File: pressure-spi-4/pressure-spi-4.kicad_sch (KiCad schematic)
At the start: 13 parts, among them J1 Conn_01x08_Male, U1 TruStability_SPI_RR, U2 TruStability_SPI_RR, U3 TruStability_SPI_RR, U4 TruStability_SPI_RN

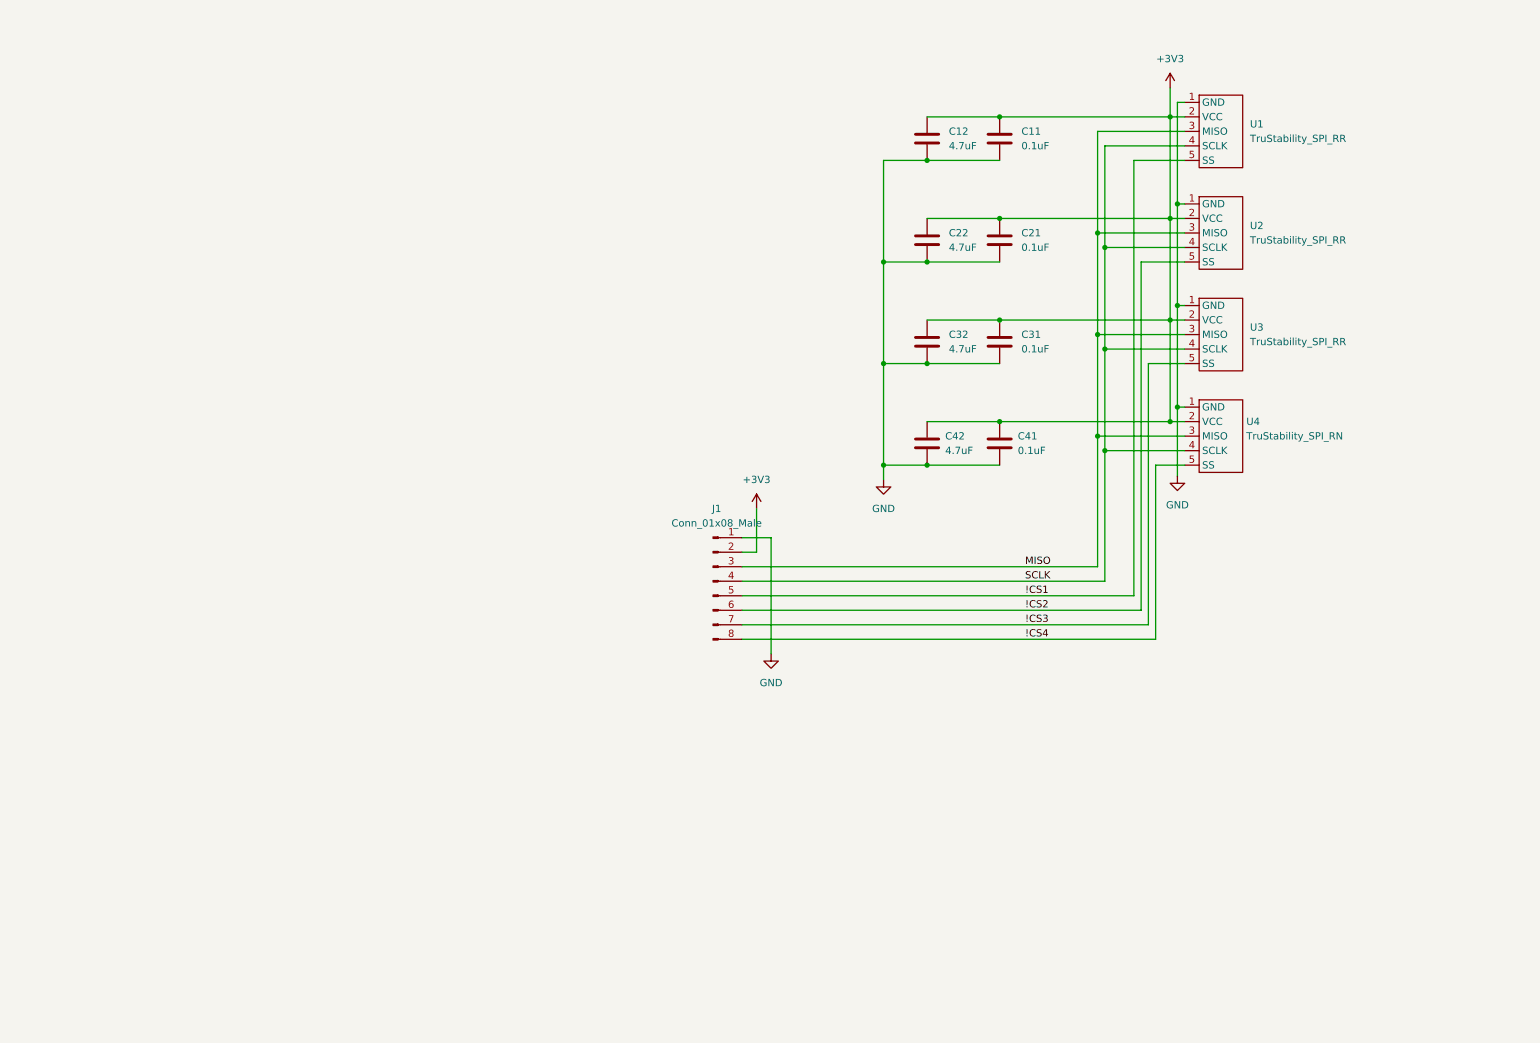
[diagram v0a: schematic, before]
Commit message: Designed and routed board.
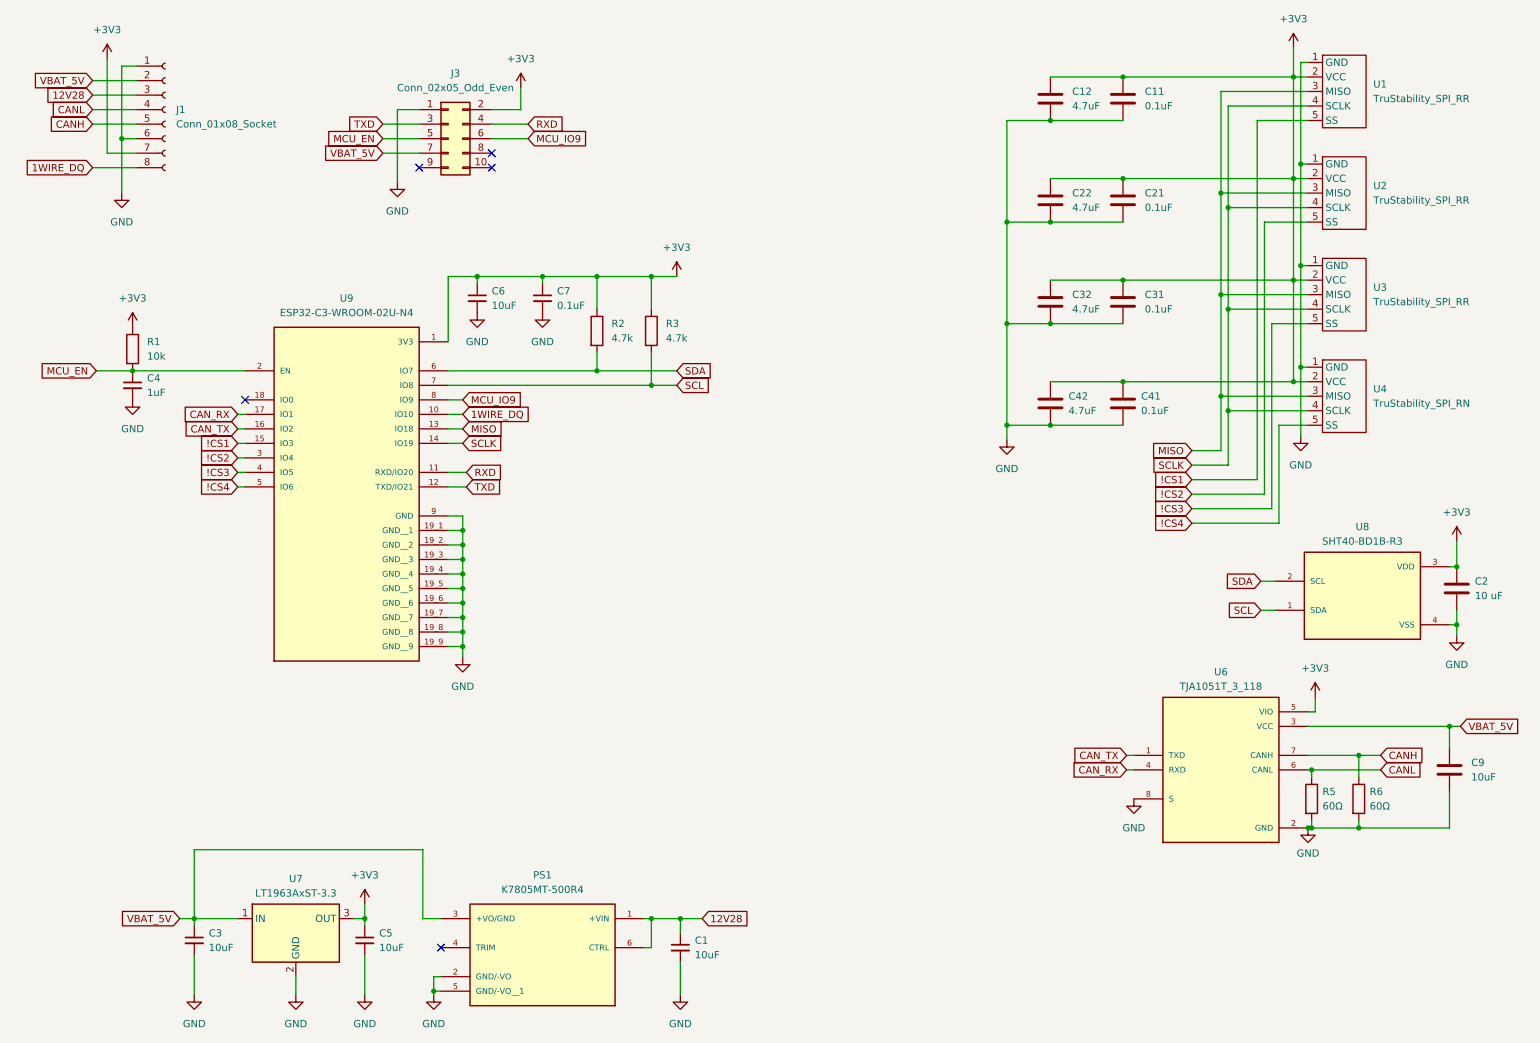
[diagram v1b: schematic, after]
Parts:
- removed J1: Conn_01x08_Male, airball-hardware:JST_SH_BM08B-SRSS-TB_1x08-1MP_P1.00mm_Vertical, symbol Connector:Conn_01x08_Male
- added C1, C3, C5, C6: 10uF, Capacitor_SMD:C_0603_1608Metric, symbol Device:C_Small
- added C2: 10 uF, Capacitor_SMD:C_0603_1608Metric, symbol Device:C
- added C4: 1uF, Capacitor_SMD:C_0603_1608Metric, symbol Device:C_Small
- added C7: 0.1uF, Capacitor_SMD:C_0603_1608Metric, symbol Device:C_Small
- added C9: 10uF, Capacitor_SMD:C_0603_1608Metric, symbol Device:C
- added J1: Conn_01x08_Socket, Connector_PinHeader_1.27mm:PinHeader_1x08_P1.27mm_Vertical, symbol Connector:Conn_01x08_Socket
- added J3: Conn_02x05_Odd_Even, Connector_PinHeader_1.27mm:PinHeader_2x05_P1.27mm_Vertical, symbol Connector_Generic:Conn_02x05_Odd_Even
- added PS1: K7805MT-500R4, airball-hardware:CONV_K7805MT-500R4, symbol airball-hardware:K7805MT-500R4
- added R1: 10k, Resistor_SMD:R_0603_1608Metric, symbol Device:R
- added R2, R3: 4.7k, Resistor_SMD:R_0603_1608Metric, symbol Device:R
- added R5, R6: 60Ω, Resistor_SMD:R_0603_1608Metric, symbol Device:R
- added U6: TJA1051T_3_118, airball-hardware:TJA1051T_3_118, symbol airball-hardware:TJA1051T_3_118
- added U7: LT1963AxST-3.3, Package_TO_SOT_SMD:SOT-223-3_TabPin2, symbol Regulator_Linear:LT1963AxST-3.3
- added U8: SHT40-BD1B-R3, airball-hardware:SHT4X humidity sensor, symbol airball-hardware:SHT40-BD1B-R3 humidity sensor
- added U9: ESP32-C3-WROOM-02U-N4, airball-hardware:XCVR_ESP32-C3-WROOM-02U-N4, symbol airball-hardware:ESP32-C3-WROOM-02U-N4
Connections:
- net !CS1: now also U9.15 (IO3)
- net !CS2: now also U9.3 (IO4)
- net !CS3: now also U9.4 (IO5)
- net !CS4: now also U9.5 (IO6)
- net +3V3: now also C2.1, C5.1, C6.1, C7.1, J1.7 (Pin_7), J3.2 (Pin_2), R1.1, R2.1, R3.1, U6.5 (VIO), U7.3 (OUT), U8.3 (VDD), U9.1 (3V3)
- net GND: now also C1.2, C2.2, C3.2, C4.2, C5.2, C6.2, C7.2, C9.2, J1.1 (Pin_1), J1.6 (Pin_6), J3.1 (Pin_1), PS1.2 (GND/-VO), PS1.5 (GND/-VO__1), R5.2, R6.2, U6.2 (GND), U6.8 (S), U7.2 (GND), U8.4 (VSS), U9.19_1 (GND__1), U9.19_2 (GND__2), U9.19_3 (GND__3), U9.19_4 (GND__4), U9.19_5 (GND__5), U9.19_6 (GND__6), U9.19_7 (GND__7), U9.19_8 (GND__8), U9.19_9 (GND__9), U9.9 (GND)
- net MISO: now also U9.13 (IO18)
- net SCLK: now also U9.14 (IO19)
- new net 12V28: C1.1, J1.3 (Pin_3), PS1.1 (+VIN), PS1.6 (CTRL)
- new net 1WIRE_DQ: J1.8 (Pin_8), U9.10 (IO10)
- new net CANH: J1.5 (Pin_5), R6.1, U6.7 (CANH)
- new net CANL: J1.4 (Pin_4), R5.1, U6.6 (CANL)
- new net CAN_RX: U6.4 (RXD), U9.17 (IO1)
- new net CAN_TX: U6.1 (TXD), U9.16 (IO2)
- new net MCU_EN: C4.1, J3.5 (Pin_5), R1.2, U9.2 (EN)
- new net MCU_IO9: J3.6 (Pin_6), U9.8 (IO9)
- new net RXD: J3.4 (Pin_4), U9.11 (RXD/IO20)
- new net SCL: R3.2, U8.1 (SDA), U9.7 (IO8)
- new net SDA: R2.2, U8.2 (SCL), U9.6 (IO7)
- new net TXD: J3.3 (Pin_3), U9.12 (TXD/IO21)
- new net VBAT_5V: C3.1, C9.1, J1.2 (Pin_2), J3.7 (Pin_7), PS1.3 (+VO/GND), U6.3 (VCC), U7.1 (IN)
- no-connect marks 0 -> 5
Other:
- moved on the sheet: C11, C12, C21, C22, C31, C32, C41, C42, U1, U2, U3, U4
